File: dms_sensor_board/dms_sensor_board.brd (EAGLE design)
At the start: 40.3 x 30.5 mm, 21 parts

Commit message: added mosfet control over DMS ON
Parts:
- added Q1: IRLML5203, ngohara_parts:MICRO3
- moved JP4 69.1 mm to (34.4, 40.3), turned to 180 degrees
- moved JP6 68.2 mm to (39.9, 17.1), turned to 270 degrees
- moved JP5 56.6 mm to (39.5, 28.6), turned to 270 degrees
- moved U$1 53.4 mm to (30.4, 3.05)
- moved JP1 43.7 mm to (4.83, 16.1), turned to 90 degrees
- moved U$2 39.6 mm to (7.87, 2.54)
- moved JP3 39.5 mm to (13.5, 40.1)
- moved R2 31.1 mm to (10.4, 19.6), turned to 270 degrees
- moved R1 27.4 mm to (10.4, 14.5), turned to 270 degrees
- moved JP2 21.8 mm to (4.70, 27.8), turned to 90 degrees
- moved U$3 2.29 mm to (-34.5, -3.81)
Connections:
- new net DMS_ON: Q1.1, U$2.P$1
- new net N$6: U$3.8
- net 5V: now also Q1.2, Q1.3
- net DATA1-L: now also U$3.13
- net DATA2-L: now also U$3.14
- net DATA3-L: now also U$3.15
- net DATA4-L: now also U$3.12
- net DATA5-L: now also U$3.1
- net DATA6-L: now also U$3.5
- net GND: now also U$3.16, U$3.2, U$3.4, U$3.7
- net N$1: now also U$3.11
- net N$2: now also U$3.10
- net N$3: now also U$3.9
- net N$4: now also U$3.6
- net N$5: now also U$3.3
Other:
- board size 40.3 x 30.5 mm -> 44.5 x 44.5 mm

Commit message: Finished dms sensor board layout, needs DRC
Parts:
- removed U$3: 8X1_ANALOG_MUX, ngohara_parts:TSSOP16
- added MUX1: 8X1, ngohara_parts:SO16
- moved R11 68.1 mm to (31.2, 17.5)
- moved R12 63.0 mm to (31.2, 15.1), turned to 180 degrees
- moved R9 61.7 mm to (31.2, 26.9)
- moved R10 58.6 mm to (31.2, 24.5), turned to 180 degrees
- moved R8 56.0 mm to (30.4, 32.8), turned to 270 degrees
- moved R5 52.9 mm to (16.6, 32.5), turned to 90 degrees
- moved R7 48.5 mm to (27.9, 32.8), turned to 90 degrees
- moved Q1 47.7 mm to (6.48, 9.27), turned to 90 degrees
- moved R4 42.7 mm to (11.9, 28.8)
- moved R3 37.4 mm to (11.9, 26.5), turned to 180 degrees
- moved R6 34.6 mm to (19.1, 32.5), turned to 270 degrees
- moved U$1 22.1 mm to (8.38, 0.38)
- moved U$2 12.5 mm to (20.2, 0.64)
- moved JP4 6.95 mm to (28.4, 36.7), turned to 0 degrees
- moved JP6 4.96 mm to (34.9, 17.4)
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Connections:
- removed net N$6: U$3.8
- new net VCC: JP1.1, JP2.1, JP3.1, JP4.1, JP5.1, JP6.1, Q1.3
- net 5V: now also MUX1.8; no longer JP1.1, JP2.1, JP3.1, JP4.1, JP5.1, JP6.1, Q1.3
- net DATA1-L: now also MUX1.13; no longer U$3.13
- net DATA2-L: now also MUX1.14; no longer U$3.14
- net DATA3-L: now also MUX1.15; no longer U$3.15
- net DATA4-L: now also MUX1.12; no longer U$3.12
- net DATA5-L: now also MUX1.1; no longer U$3.1
- net DATA6-L: now also MUX1.5; no longer U$3.5
- net GND: now also MUX1.16, MUX1.2, MUX1.4, MUX1.7; no longer U$3.16, U$3.2, U$3.4, U$3.7
- net N$1: now also MUX1.11; no longer U$3.11
- net N$2: now also MUX1.10; no longer U$3.10
- net N$3: now also MUX1.9; no longer U$3.9
- net N$4: now also MUX1.6; no longer U$3.6
- net N$5: now also MUX1.3; no longer U$3.3
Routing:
- net VCC: track 0.00 -> 100.3 mm
- net N$5: track 0.00 -> 40.8 mm, vias 0 -> 2
- net DMS_ON: track 0.00 -> 28.4 mm
- net DATA3-L: track 0.00 -> 22.3 mm
- net DATA1-L: track 0.00 -> 20.6 mm, vias 0 -> 2
- net DATA4-L: track 0.00 -> 20.6 mm
- net 5V: track 0.00 -> 20.1 mm
- net DATA2-L: track 0.00 -> 20.1 mm, vias 0 -> 2
- net DATA5-L: track 0.00 -> 18.9 mm, vias 0 -> 2
- net N$4: track 0.00 -> 18.4 mm
- net N$1: track 0.00 -> 16.0 mm
- net DATA6-L: track 0.00 -> 14.9 mm, vias 0 -> 2
- net N$2: track 0.00 -> 13.8 mm
- net N$3: track 0.00 -> 11.4 mm
- net DATA3-H: track 0.00 -> 3.59 mm
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- added copper zone on layer 1, net GND
- added copper zone on layer 16, net GND

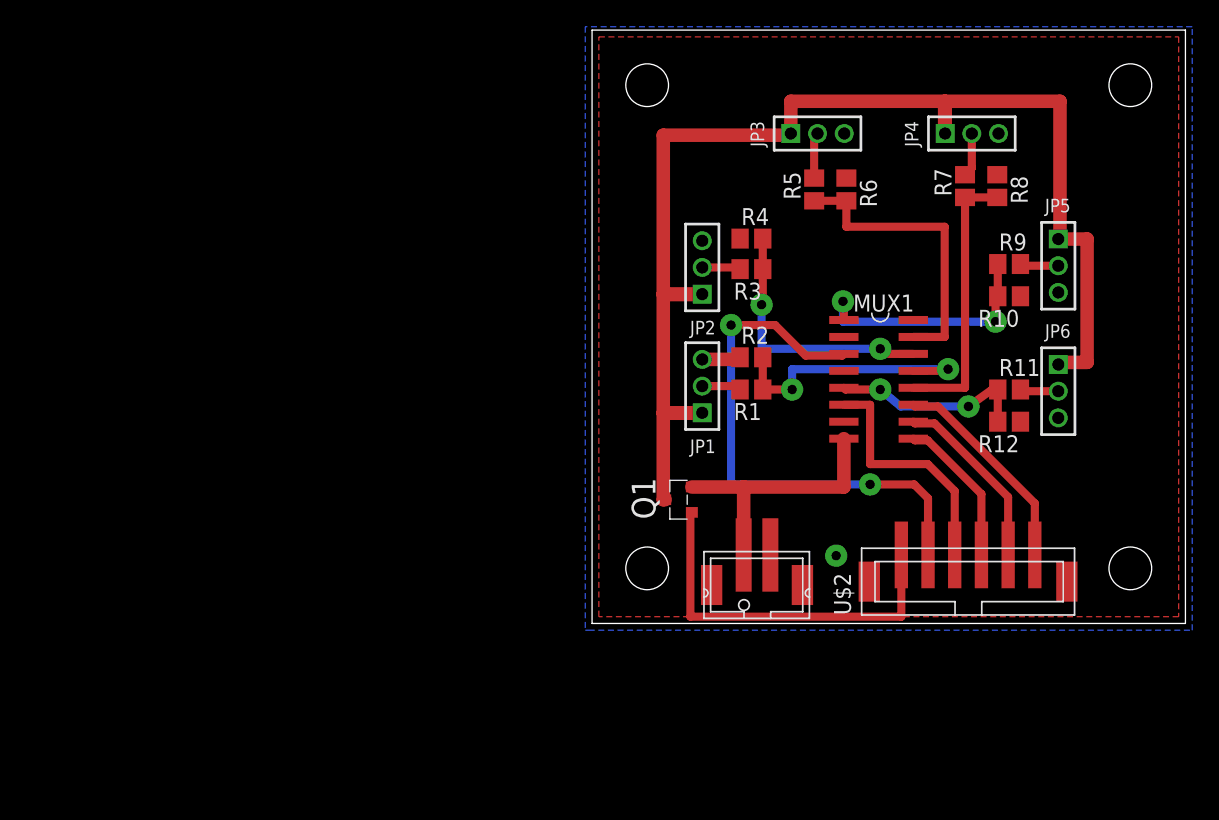
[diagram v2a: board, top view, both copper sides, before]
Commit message: Fixed DMS_on fet with resistors and finished text
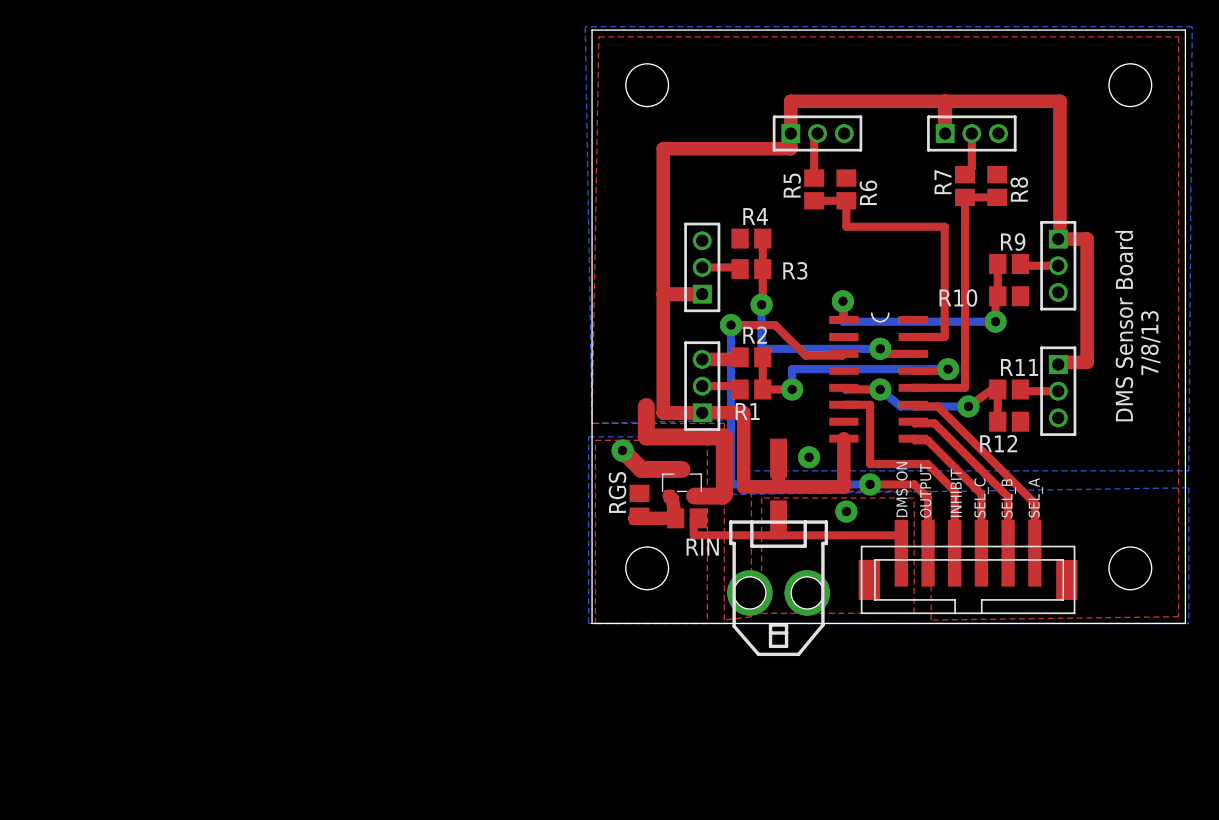
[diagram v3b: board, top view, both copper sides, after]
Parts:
- removed U$1: JST-PH2-SMD, jst-ph:JST-PH2-SMD
- added RGS, RIN: (no value), resistor:R0805
- added X1: (no value), con-molex-micro-fit-3_0:43045-0206
- moved Q1 1.30 mm to (6.73, 10.5), turned to 0 degrees
- moved U$2 0.13 mm to (20.2, 0.76)
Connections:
- removed net VCC: JP1.1, JP2.1, JP3.1, JP4.1, JP5.1, JP6.1, Q1.3
- new net N$8: Q1.1, RGS.1, RIN.2
- new net N_GND: JP1.3, JP2.3, JP3.3, JP4.3, JP5.3, JP6.3, MUX1.16, MUX1.2, MUX1.4, MUX1.7, Q1.2, R10.1, R12.1, R2.1, R4.1, R6.1, R8.1
- net 5V: now also JP1.1, JP2.1, JP3.1, JP4.1, JP5.1, JP6.1, X1.P$2; no longer Q1.2, U$1.P$1
- net DMS_ON: now also RIN.1; no longer Q1.1
- net GND: now also Q1.3, RGS.2, X1.P$1; no longer JP1.3, JP2.3, JP3.3, JP4.3, JP5.3, JP6.3, MUX1.16, MUX1.2, MUX1.4, MUX1.7, R10.1, R12.1, R2.1, R4.1, R6.1, R8.1, U$1.P$2
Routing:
- net VCC: track 100.3 -> 0.00 mm
- net 5V: track 20.1 -> 115.7 mm
- net N_GND: track 0.00 -> 17.4 mm, vias 0 -> 1
- net DMS_ON: track 28.4 -> 18.4 mm
- net N$8: track 0.00 -> 5.21 mm
- net GND: track 2.90 -> 5.28 mm, vias 1 -> 2
- added copper zone on layer 1, net N_GND
- added copper zone on layer 16, net N_GND
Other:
- board text added: "DMS Sensor Board 7/8/13"
- board text added: "DMS_ON"
- board text added: "INHIBIT"
- board text added: "OUTPUT"
- board text added: "SEL_A"
- board text added: "SEL_B"
- board text added: "SEL_C"

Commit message: resolved Sparkfun DRC errors, except for in-between pin errors
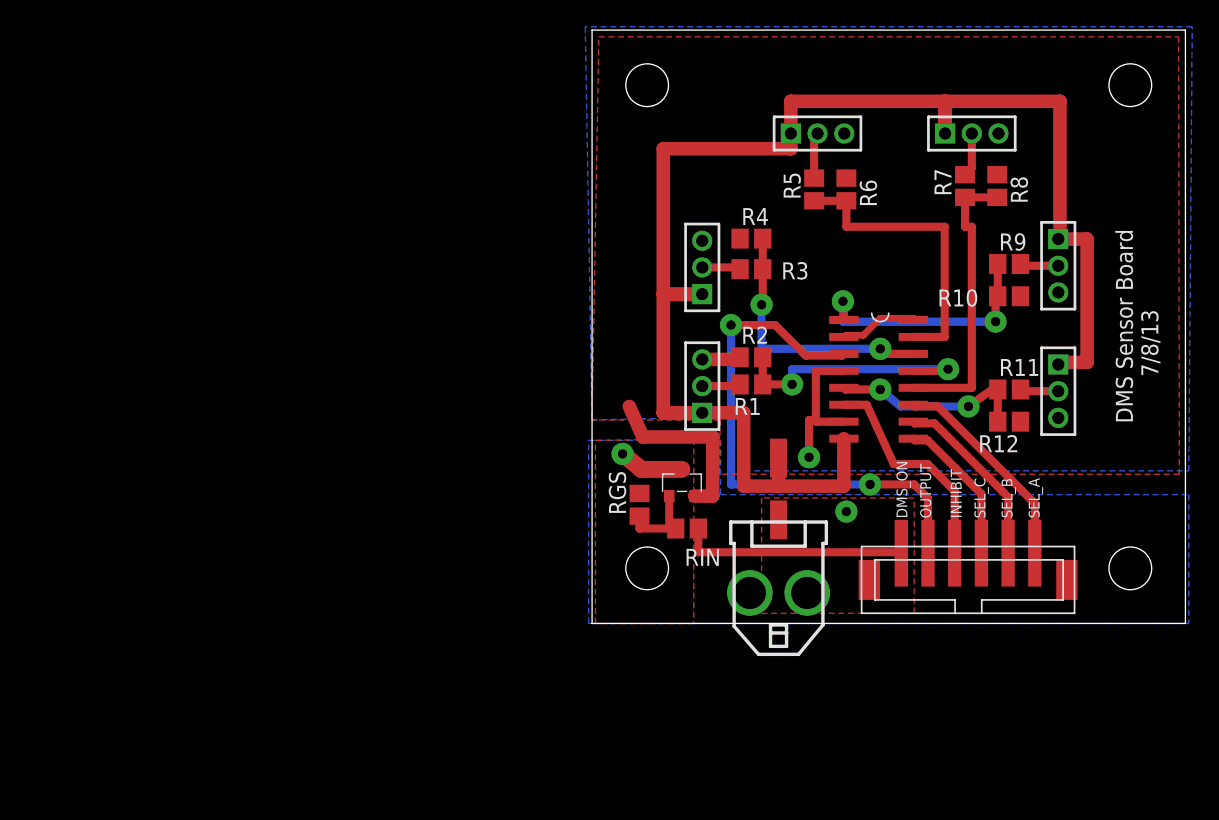
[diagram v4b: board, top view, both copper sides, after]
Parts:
- moved RIN 0.76 mm to (7.11, 7.11)
- moved R1 0.38 mm to (11.9, 17.9)
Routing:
- net N_GND: track 17.4 -> 33.5 mm
- net N$4: track 18.2 -> 16.7 mm
- net DMS_ON: track 18.4 -> 17.1 mm
- net N$8: track 5.21 -> 6.54 mm
- net DATA4-L: track 20.6 -> 21.6 mm
- net DATA1-L: track 20.6 -> 19.8 mm

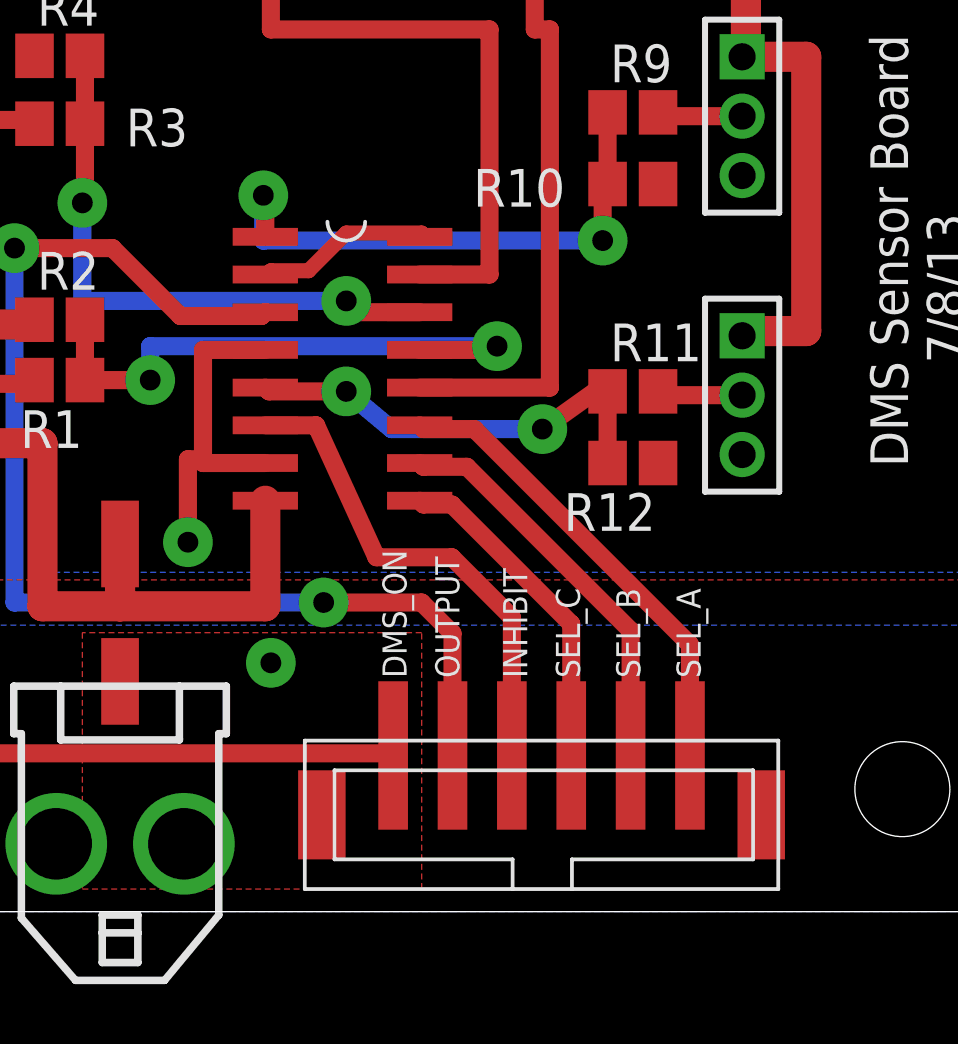
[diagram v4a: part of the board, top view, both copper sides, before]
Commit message: mostly silkscreen fixes
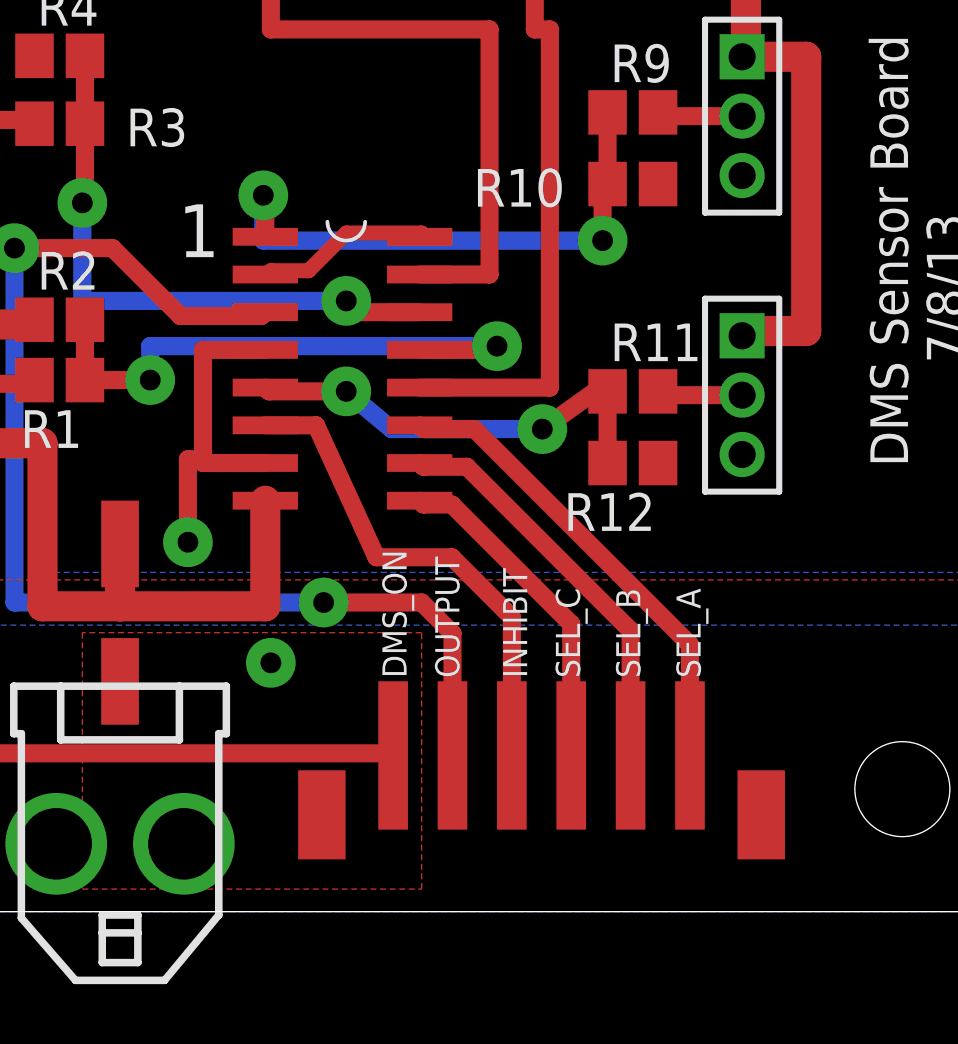
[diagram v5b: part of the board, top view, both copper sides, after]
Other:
- board text added: "1"
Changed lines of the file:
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@@
 <layer number="37" name="tTest" color="7" fill="1" visible="no" active="yes"/>
 <layer number="38" name="bTest" color="7" fill="1" visible="no" active="yes"/>
-<layer number="39" name="tKeepout" color="4" fill="11" visible="yes" active="yes"/>
-<layer number="40" name="bKeepout" color="1" fill="11" visible="yes" active="yes"/>
-<layer number="41" name="tRestrict" color="4" fill="10" visible="yes" active="yes"/>
-<layer number="42" name="bRestrict" color="1" fill="10" visible="yes" active="yes"/>
-<layer number="43" name="vRestrict" color="2" fill="10" visible="yes" active="yes"/>
+<layer number="39" name="tKeepout" color="4" fill="11" visible="no" active="yes"/>
+<layer number="40" name="bKeepout" color="1" fill="11" visible="no" active="yes"/>
+<layer number="41" name="tRestrict" color="4" fill="10" visible="no" active="yes"/>
+<layer number="42" name="bRestrict" color="1" fill="10" visible="no" active="yes"/>
+<layer number="43" name="vRestrict" color="2" fill="10" visible="no" active="yes"/>
 <layer number="44" name="Drills" color="7" fill="1" visible="no" active="yes"/>
-<layer number="45" name="Holes" color="7" fill="1" visible="yes" active="yes"/>
+<layer number="45" name="Holes" color="7" fill="1" visible="no" active="yes"/>
 <layer number="46" name="Milling" color="3" fill="1" visible="no" active="yes"/>
 <layer number="47" name="Measures" color="7" fill="1" visible="no" active="yes"/>
-<layer number="48" name="Document" color="7" fill="1" visible="yes" active="yes"/>
-<layer number="49" name="Reference" color="7" fill="1" visible="yes" active="yes"/>
+<layer number="48" name="Document" color="7" fill="1" visible="no" active="yes"/>
+<layer number="49" name="Reference" color="7" fill="1" visible="no" active="yes"/>
 <layer number="50" name="dxf" color="7" fill="1" visible="no" active="no"/>
-<layer number="51" name="tDocu" color="7" fill="1" visible="yes" active="yes"/>
-<layer number="52" name="bDocu" color="7" fill="1" visible="yes" active="yes"/>
+<layer number="51" name="tDocu" color="7" fill="1" visible="no" active="yes"/>
+<layer number="52" name="bDocu" color="7" fill="1" visible="no" active="yes"/>
 <layer number="53" name="tGND_GNDA" color="7" fill="9" visible="no" active="no"/>
 <layer number="54" name="bGND_GNDA" color="1" fill="9" visible="no" active="no"/>
@@
 <layer number="106" name="bPlate" color="7" fill="1" visible="no" active="yes"/>
 <layer number="107" name="Crop" color="7" fill="1" visible="no" active="yes"/>
-<layer number="108" name="tplace-old" color="10" fill="1" visible="yes" active="yes"/>
-<layer number="109" name="ref-old" color="11" fill="1" visible="yes" active="yes"/>
+<layer number="108" name="tplace-old" color="10" fill="1" visible="no" active="yes"/>
+<layer number="109" name="ref-old" color="11" fill="1" visible="no" active="yes"/>
 <layer number="116" name="Patch_BOT" color="9" fill="4" visible="no" active="yes"/>
-<layer number="121" name="_tsilk" color="7" fill="1" visible="yes" active="yes"/>
+<layer number="121" name="_tsilk" color="7" fill="1" visible="no" active="yes"/>
 <layer number="122" name="_bsilk" color="7" fill="1" visible="no" active="yes"/>
 <layer number="125" name="_tNames" color="7" fill="1" visible="no" active="yes"/>
-<layer number="144" name="Drill_legend" color="7" fill="1" visible="yes" active="yes"/>
+<layer number="144" name="Drill_legend" color="7" fill="1" visible="no" active="yes"/>
 <layer number="151" name="HeatSink" color="7" fill="1" visible="no" active="yes"/>
-<layer number="199" name="Contour" color="7" fill="1" visible="yes" active="yes"/>
+<layer number="199" name="Contour" color="7" fill="1" visible="no" active="yes"/>
 <layer number="200" name="200bmp" color="1" fill="10" visible="no" active="yes"/>
 <layer number="201" name="201bmp" color="2" fill="10" visible="no" active="yes"/>
@@
 <text x="42.418" y="14.986" size="1.27" layer="25" rot="R90">DMS Sensor Board
        7/8/13</text>
+<text x="15.9258" y="22.0472" size="1.778" layer="25">1</text>
 </plain>
 <attributes>
